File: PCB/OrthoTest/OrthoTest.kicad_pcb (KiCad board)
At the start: 2 copper layers, 3.6 x 3.3 mm, 182 parts, among them SW1 SW_Push, SW10 SW_Push, SW11 SW_Push, SW12 SW_Push, SW13 SW_Push, SW14 SW_Push, SW15 SW_Push, SW16 SW_Push, SW17 SW_Push, SW18 SW_Push, SW19 SW_Push, SW2 SW_Push, SW20 SW_Push, SW21 SW_Push, SW22 SW_Push, SW23 SW_Push, SW24 SW_Push, SW25 SW_Push, SW26 SW_Push, SW27 SW_Push, SW28 SW_Push, SW29 SW_Push, SW3 SW_Push, SW30 SW_Push, SW31 SW_Push, SW32 SW_Push, SW33 SW_Push, SW34 SW_Push, SW35 SW_Push, SW36 SW_Push, SW37 SW_Push, SW38 SW_Push, SW39 SW_Push, SW4 SW_Push, SW40 SW_Push, SW41 SW_Push, SW42 SW_Push, SW43 SW_Push, SW44 SW_Push, SW45 SW_Push, SW46 SW_Push, SW47 SW_Push, SW48 SW_Push, SW49 SW_Push, SW5 SW_Push, SW50 SW_Push, SW51 SW_Push, SW52 SW_Push, SW53 SW_Push, SW54 SW_Push, SW55 SW_Push, SW56 SW_Push, SW57 SW_Push, SW58 SW_Push, SW59 SW_Push, SW6 SW_Push, SW60 RotaryEncoder_Switch_MP, SW61 RotaryEncoder_Switch_MP, SW7 SW_Push, SW8 SW_Push, SW9 SW_Push

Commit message: added libraries and placed pcb components
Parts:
- A1: footprint Module:RaspberryPi_Pico_Common_SMD -> Module:RaspberryPi_Pico_Common_THT
- D1, D10, D11, D12, D13, D14, D15, D16, D17, D18, D19, D2, D20, D21, D22, D23, D24, D25, D26, D27, D28, D29, D3, D30, D31, D32, D33, D34, D35, D36, D37, D38, D39, D4, D40, D41, D42, D43, D44, D45, D46, D47, D48, D49, D5, D50, D51, D52, D53, D54, D55, D56, D57, D58, D59, D6, D7, D8, D9, LED1, LED10, LED11, LED12, LED13, LED14, LED15, LED16, LED17, LED18, LED19, LED2, LED20, LED21, LED22, LED23, LED24, LED25, LED26, LED27, LED28, LED29, LED3, LED30, LED31, LED32, LED33, LED34, LED35, LED36, LED37, LED38, LED39, LED4, LED40, LED41, LED42, LED43, LED44, LED45, LED46, LED47, LED48, LED49, LED5, LED50, LED51, LED52, LED53, LED54, LED55, LED56, LED57, LED58, LED59, LED6, LED7, LED8, LED9: moved to B.Cu
- moved LED12 447.3 mm to (251.4, 36.6)
- moved LED24 432.7 mm to (251.4, 55.7)
- moved LED11 427.7 mm to (232.3, 36.6)
- moved LED36 418.7 mm to (251.4, 74.8)
- moved LED23 413.0 mm to (232.3, 55.7)
- moved LED10 408.0 mm to (213.3, 36.6)
- moved LED48 405.3 mm to (251.4, 93.8)
- moved D12 400.7 mm to (255.8, 49.1), turned to 135 degrees
- moved LED35 399.0 mm to (232.3, 74.8)
- moved LED22 393.4 mm to (213.3, 55.7)
- moved LED59 391.6 mm to (251.4, 112.8)
- moved D24 389.9 mm to (255.8, 68.2), turned to 135 degrees
- moved LED9 388.4 mm to (194.2, 36.6)
- moved SW48 386.2 mm to (251.3, 98.5)
- moved SW12 386.1 mm to (251.3, 41.4)
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- renumbered S1 to S54
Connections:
- SW60 pad A: unconnected-(SW60-PadA) -> (no net)
- SW60 pad B: unconnected-(SW60-PadB) -> (no net)
- SW60 pad C: GND -> (no net)
- SW60 pad MP: unconnected-(SW60-PadMP) -> (no net)
- SW60 pad S1: unconnected-(SW60-PadS1) -> (no net)
- SW60 pad S2: unconnected-(SW60-PadS2) -> (no net)
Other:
- board size 3.6 x 3.3 mm -> 228.6 x 127.2 mm
- board text added: "Raspberry Pi Pico"

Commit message: finished routing pcb
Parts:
- added D60: D, MyKeebLib:D_SOD-123_SmallArrow, F.Cu at (266.0, 34.1)
- added D61: D, MyKeebLib:D_SOD-123_SmallArrow, F.Cu at (236.9, 34.1)
- moved D40 27.7 mm to (113.2, 132.2)
- moved D42 27.7 mm to (151.2, 132.2)
- moved D43 27.7 mm to (170.3, 132.2)
- moved D45 27.7 mm to (208.4, 132.2)
- moved D47 27.7 mm to (246.5, 132.2)
- moved D48 27.7 mm to (265.6, 132.2)
- moved LED26 27.7 mm to (70.7, 100.7)
- moved LED30 27.7 mm to (146.9, 100.7)
- moved LED32 27.7 mm to (185.0, 100.7)
- moved LED33 27.7 mm to (204.1, 100.7)
- moved LED35 27.7 mm to (242.2, 100.7)
- moved LED38 27.7 mm to (70.7, 119.7)
- moved LED42 27.7 mm to (146.9, 119.7)
- moved LED44 27.7 mm to (185.0, 119.7)
- moved LED45 27.7 mm to (204.1, 119.7)
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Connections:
- A1 pad 1: unconnected-(A1-GPIO0-Pad1) -> col0
- A1 pad 10: unconnected-(A1-GPIO7-Pad10) -> col7
- A1 pad 11: unconnected-(A1-GPIO8-Pad11) -> col8
- A1 pad 12: unconnected-(A1-GPIO9-Pad12) -> col9
- A1 pad 13: Net-(A1-GND-Pad13) -> GND
- A1 pad 14: unconnected-(A1-GPIO10-Pad14) -> col10
- A1 pad 15: unconnected-(A1-GPIO11-Pad15) -> col11
- A1 pad 16: unconnected-(A1-GPIO12-Pad16) -> ec1_b
- A1 pad 17: unconnected-(A1-GPIO13-Pad17) -> ec1_a
- A1 pad 18: Net-(A1-GND-Pad13) -> GND
- A1 pad 19: unconnected-(A1-GPIO14-Pad19) -> ec2_a
- A1 pad 2: unconnected-(A1-GPIO1-Pad2) -> col1
- A1 pad 20: unconnected-(A1-GPIO15-Pad20) -> ec2_b
- A1 pad 21: unconnected-(A1-GPIO16-Pad21) -> oled_cl
- A1 pad 22: unconnected-(A1-GPIO17-Pad22) -> oled_data
- A1 pad 23: Net-(A1-GND-Pad13) -> GND
- A1 pad 24: unconnected-(A1-GPIO18-Pad24) -> ec_col0
- A1 pad 25: unconnected-(A1-GPIO19-Pad25) -> ec_col1
- A1 pad 26: unconnected-(A1-GPIO20-Pad26) -> ec_row0
- A1 pad 27: unconnected-(A1-GPIO21-Pad27) -> row4
- A1 pad 28: Net-(A1-GND-Pad13) -> GND
- A1 pad 29: unconnected-(A1-GPIO22-Pad29) -> row3
- A1 pad 3: Net-(A1-GND-Pad13) -> GND
- A1 pad 31: unconnected-(A1-GPIO26_ADC0-Pad31) -> row2
- A1 pad 32: unconnected-(A1-GPIO27_ADC1-Pad32) -> row1
- A1 pad 33: unconnected-(A1-AGND-Pad33) -> GND
- A1 pad 34: unconnected-(A1-GPIO28_ADC2-Pad34) -> row0
- A1 pad 35: unconnected-(A1-ADC_VREF-Pad35) -> led_data
- A1 pad 36: unconnected-(A1-3V3-Pad36) -> +3V3
- A1 pad 38: Net-(A1-GND-Pad13) -> GND
- A1 pad 4: unconnected-(A1-GPIO2-Pad4) -> col2
- A1 pad 40: unconnected-(A1-VBUS-Pad40) -> +5V
- A1 pad 5: unconnected-(A1-GPIO3-Pad5) -> col3
- A1 pad 6: unconnected-(A1-GPIO4-Pad6) -> col4
- A1 pad 7: unconnected-(A1-GPIO5-Pad7) -> col5
- A1 pad 8: Net-(A1-GND-Pad13) -> GND
- A1 pad 9: unconnected-(A1-GPIO6-Pad9) -> col6
- SW60 pad A: (no net) -> ec1_a
- SW60 pad B: (no net) -> ec1_b
- SW60 pad C: (no net) -> GND
- SW60 pad MP: (no net) -> GND
- SW60 pad S1: (no net) -> ec_col0
- SW60 pad S2: (no net) -> Net-(D60-A)
- SW61 pad A: unconnected-(SW61-PadA) -> ec2_a
- SW61 pad B: unconnected-(SW61-PadB) -> ec2_b
- SW61 pad MP: unconnected-(SW61-PadMP) -> GND
- SW61 pad S1: unconnected-(SW61-PadS1) -> ec_col1
- SW61 pad S2: unconnected-(SW61-PadS2) -> Net-(D61-A)
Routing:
- net +5V: track 0.00 -> 1596.4 mm, vias 0 -> 61
- net row4: track 0.00 -> 350.5 mm, vias 0 -> 8
- net row3: track 0.00 -> 329.8 mm, vias 0 -> 6
- net row2: track 0.00 -> 315.1 mm, vias 0 -> 4
- net row1: track 0.00 -> 298.0 mm, vias 0 -> 2
- net row0: track 0.00 -> 283.2 mm
- net col11: track 0.00 -> 276.4 mm
- net col10: track 0.00 -> 260.2 mm
- net col9: track 0.00 -> 246.3 mm
- net Net-(LED48-DOUT): track 0.00 -> 246.2 mm, vias 0 -> 2
- net Net-(LED36-DOUT): track 0.00 -> 245.3 mm, vias 0 -> 2
- net Net-(LED24-DOUT): track 0.00 -> 244.9 mm, vias 0 -> 2
- net Net-(LED12-DOUT): track 0.00 -> 244.0 mm, vias 0 -> 2
- net col8: track 0.00 -> 230.1 mm
- net col7: track 0.00 -> 214.0 mm
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- added copper zone on B.Cu, net GND
- added copper zone on F.Cu, net GND

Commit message: fixed ucontroller usb c position and added grounding vias
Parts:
- added C1: 100n, Capacitor_SMD:C_0603_1608Metric, B.Cu at (56.1, 65.9)
- added C10: 100n, Capacitor_SMD:C_0603_1608Metric, B.Cu at (227.6, 65.9)
- added C11: 100n, Capacitor_SMD:C_0603_1608Metric, B.Cu at (246.6, 65.9)
- added C12: 100n, Capacitor_SMD:C_0603_1608Metric, B.Cu at (265.0, 67.2)
- added C13: 100n, Capacitor_SMD:C_0603_1608Metric, B.Cu at (56.1, 85.0)
- added C14: 100n, Capacitor_SMD:C_0603_1608Metric, B.Cu at (75.2, 85.0)
- added C15: 100n, Capacitor_SMD:C_0603_1608Metric, B.Cu at (94.2, 85.0)
- added C16: 100n, Capacitor_SMD:C_0603_1608Metric, B.Cu at (113.2, 85.0)
- added C17: 100n, Capacitor_SMD:C_0603_1608Metric, B.Cu at (132.3, 85.0)
- added C18: 100n, Capacitor_SMD:C_0603_1608Metric, B.Cu at (151.3, 85.0)
- added C19: 100n, Capacitor_SMD:C_0603_1608Metric, B.Cu at (170.4, 85.0)
- added C2: 100n, Capacitor_SMD:C_0603_1608Metric, B.Cu at (75.2, 65.9)
- added C20: 100n, Capacitor_SMD:C_0603_1608Metric, B.Cu at (189.4, 85.0)
- added C21: 100n, Capacitor_SMD:C_0603_1608Metric, B.Cu at (208.5, 85.0)
- added C22: 100n, Capacitor_SMD:C_0603_1608Metric, B.Cu at (227.6, 85.0)
- added C23: 100n, Capacitor_SMD:C_0603_1608Metric, B.Cu at (246.6, 85.0)
- added C24: 100n, Capacitor_SMD:C_0603_1608Metric, B.Cu at (265.0, 86.3)
- added C25: 100n, Capacitor_SMD:C_0603_1608Metric, B.Cu at (56.1, 104.0)
- added C26: 100n, Capacitor_SMD:C_0603_1608Metric, B.Cu at (75.2, 104.0)
- added C27: 100n, Capacitor_SMD:C_0603_1608Metric, B.Cu at (94.2, 104.0)
- added C28: 100n, Capacitor_SMD:C_0603_1608Metric, B.Cu at (113.2, 104.0)
- added C29: 100n, Capacitor_SMD:C_0603_1608Metric, B.Cu at (132.3, 104.0)
- added C3: 100n, Capacitor_SMD:C_0603_1608Metric, B.Cu at (94.2, 65.9)
- added C30: 100n, Capacitor_SMD:C_0603_1608Metric, B.Cu at (151.3, 104.0)
- added C31: 100n, Capacitor_SMD:C_0603_1608Metric, B.Cu at (170.4, 104.0)
- added C32: 100n, Capacitor_SMD:C_0603_1608Metric, B.Cu at (189.4, 104.0)
- added C33: 100n, Capacitor_SMD:C_0603_1608Metric, B.Cu at (208.5, 104.0)
- added C34: 100n, Capacitor_SMD:C_0603_1608Metric, B.Cu at (227.6, 104.0)
- added C35: 100n, Capacitor_SMD:C_0603_1608Metric, B.Cu at (246.6, 104.0)
- added C36: 100n, Capacitor_SMD:C_0603_1608Metric, B.Cu at (265.0, 105.3)
- added C37: 100n, Capacitor_SMD:C_0603_1608Metric, B.Cu at (56.1, 123.0)
- added C38: 100n, Capacitor_SMD:C_0603_1608Metric, B.Cu at (75.2, 123.0)
- added C39: 100n, Capacitor_SMD:C_0603_1608Metric, B.Cu at (94.2, 123.0)
- added C4: 100n, Capacitor_SMD:C_0603_1608Metric, B.Cu at (113.2, 65.9)
- added C40: 100n, Capacitor_SMD:C_0603_1608Metric, B.Cu at (113.2, 123.0)
- added C41: 100n, Capacitor_SMD:C_0603_1608Metric, B.Cu at (132.3, 123.0)
- added C42: 100n, Capacitor_SMD:C_0603_1608Metric, B.Cu at (151.3, 123.0)
- added C43: 100n, Capacitor_SMD:C_0603_1608Metric, B.Cu at (170.4, 123.0)
- added C44: 100n, Capacitor_SMD:C_0603_1608Metric, B.Cu at (189.4, 123.0)
- added C45: 100n, Capacitor_SMD:C_0603_1608Metric, B.Cu at (208.5, 123.0)
- added C46: 100n, Capacitor_SMD:C_0603_1608Metric, B.Cu at (227.6, 123.0)
- added C47: 100n, Capacitor_SMD:C_0603_1608Metric, B.Cu at (246.6, 123.0)
- added C48: 100n, Capacitor_SMD:C_0603_1608Metric, B.Cu at (265.0, 124.4)
- added C49: 100n, Capacitor_SMD:C_0603_1608Metric, B.Cu at (56.1, 142.1)
- added C5: 100n, Capacitor_SMD:C_0603_1608Metric, B.Cu at (132.3, 65.9)
- added C50: 100n, Capacitor_SMD:C_0603_1608Metric, B.Cu at (75.2, 142.1)
- added C51: 100n, Capacitor_SMD:C_0603_1608Metric, B.Cu at (94.2, 142.1)
- added C52: 100n, Capacitor_SMD:C_0603_1608Metric, B.Cu at (113.2, 142.1)
- added C53: 100n, Capacitor_SMD:C_0603_1608Metric, B.Cu at (132.3, 142.1)
- added C54: 100n, Capacitor_SMD:C_0603_1608Metric, B.Cu at (160.9, 142.1)
- added C55: 100n, Capacitor_SMD:C_0603_1608Metric, B.Cu at (189.4, 142.1)
- added C56: 100n, Capacitor_SMD:C_0603_1608Metric, B.Cu at (208.5, 142.1)
- added C57: 100n, Capacitor_SMD:C_0603_1608Metric, B.Cu at (227.6, 142.1)
- added C58: 100n, Capacitor_SMD:C_0603_1608Metric, B.Cu at (246.6, 142.1)
- added C59: 100n, Capacitor_SMD:C_0603_1608Metric, B.Cu at (265.6, 142.1)
- added C6: 100n, Capacitor_SMD:C_0603_1608Metric, B.Cu at (151.3, 65.9)
- added C7: 100n, Capacitor_SMD:C_0603_1608Metric, B.Cu at (170.4, 65.9)
- added C8: 100n, Capacitor_SMD:C_0603_1608Metric, B.Cu at (189.4, 65.9)
- added C9: 100n, Capacitor_SMD:C_0603_1608Metric, B.Cu at (208.5, 65.9)
- added H1: MountingHolePlate, MyKeebLib:Spacer_3.2mm, F.Cu at (80.2, 86.3)
- added H2: MountingHolePlate, MyKeebLib:Spacer_3.2mm, F.Cu at (80.2, 124.4)
- added H3: MountingHolePlate, MyKeebLib:Spacer_3.2mm, F.Cu at (156.4, 86.3)
- added H4: MountingHolePlate, MyKeebLib:Spacer_3.2mm, F.Cu at (156.4, 128.4)
- added H5: MountingHolePlate, MyKeebLib:Spacer_3.2mm, F.Cu at (232.6, 86.3)
- added H6: MountingHolePlate, MyKeebLib:Spacer_3.2mm, F.Cu at (232.6, 124.4)
- moved A1 5.00 mm to (38.7, 53.3)
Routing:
- net +5V: track 1596.4 -> 1756.8 mm
- net oled_data: track 89.1 -> 94.1 mm
- net oled_cl: track 85.5 -> 90.5 mm
- net ec1_b: track 175.7 -> 180.7 mm
- net ec1_a: track 174.9 -> 179.9 mm
- net ec2_b: track 135.8 -> 140.8 mm
- net +3V3: track 138.0 -> 143.0 mm
- net ec2_a: track 141.7 -> 146.4 mm
- net ec_col1: track 163.8 -> 168.2 mm
- net ec_col0: track 198.1 -> 202.5 mm
- net ec_row0: track 190.1 -> 194.4 mm
- net col11: track 276.4 -> 280.6 mm
- net col10: track 260.2 -> 264.1 mm
- net col9: track 246.3 -> 250.0 mm
- net row3: track 329.8 -> 333.5 mm
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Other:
- board size 228.6 x 127.2 mm -> 233.7 x 127.2 mm

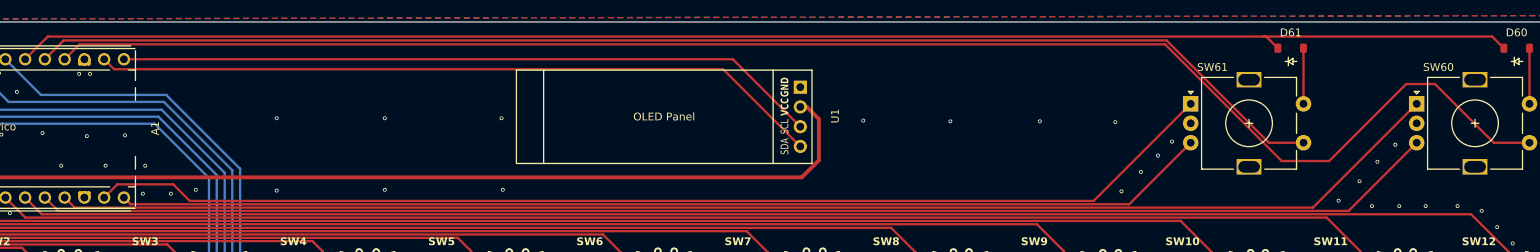
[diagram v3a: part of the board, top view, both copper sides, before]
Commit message: spaced encoders additional 10mm aparart
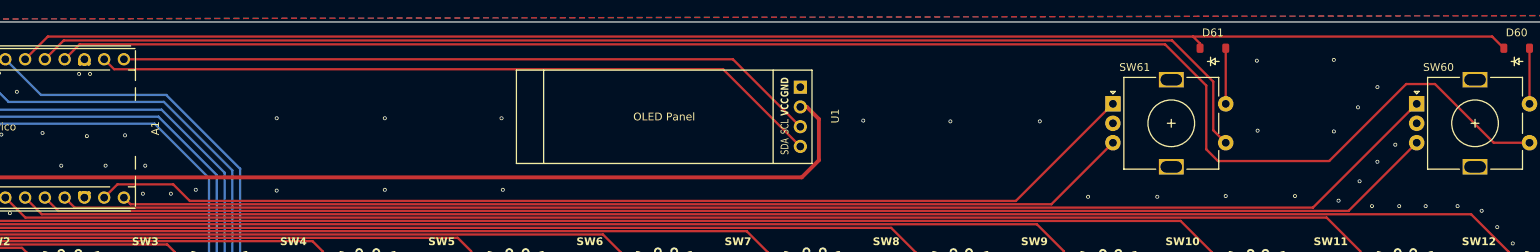
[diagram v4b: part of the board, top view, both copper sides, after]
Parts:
- moved D61 10.0 mm to (226.9, 34.1)
- moved SW61 10.0 mm to (214.1, 41.2)
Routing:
- net ec2_a: track 146.4 -> 136.4 mm
- net ec2_b: track 140.8 -> 130.8 mm
- net ec_col1: track 168.2 -> 161.9 mm
- net ec_col0: track 202.5 -> 207.3 mm
- net ec_row0: track 194.4 -> 193.8 mm
- net GND: vias 313 -> 318
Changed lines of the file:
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@@
 	(footprint "MyKeebLib:D_SOD-123_SmallArrow"
 		(layer "F.Cu")
-		(at 236.95 34.1)
+		(at 226.95 34.1)
 		(descr "SOD-123")
 		(tags "SOD-123")
@@
 	(footprint "Rotary_Encoder:RotaryEncoder_Alps_EC11E-Switch_Vertical_H20mm"
 		(layer "F.Cu")
-		(at 224.1 41.25)
+		(at 214.1 41.25)
 		(descr "Alps rotary encoder, EC12E... with switch, vertical shaft, http://www.alps.com/prod/info/E/HTML/Encoder/Incremental/EC11/EC11E15204A3.html")
 		(tags "rotary encoder")
@@
 	)
 	(segment
-		(start 267.65 46.25)
-		(end 263.05 46.25)
+		(start 226.1 38.9)
+		(end 220.8 33.6)
+		(width 0.3)
+		(layer "F.Cu")
+		(net 3)
+	)
+	(segment
+		(start 263.05 46.25)
+		(end 255.5 38.7)
+		(width 0.3)
+		(layer "F.Cu")
+		(net 3)
+	)
+	(segment
+		(start 255.5 38.7)
+		(end 251.8 38.7)
 		(width 0.3)
 		(layer "F.Cu")
@@
 	)
 	(segment
-		(start 220.8 33.6)
-		(end 81.26 33.6)
+		(start 226.1 47.1)
+		(end 226.1 38.9)
 		(width 0.3)
 		(layer "F.Cu")
@@
 	)
 	(segment
-		(start 263.05 46.25)
-		(end 255.5 38.7)
+		(start 267.65 46.25)
+		(end 263.05 46.25)
 		(width 0.3)
 		(layer "F.Cu")
@@
 	)
 	(segment
-		(start 235.8 48.6)
-		(end 220.8 33.6)
+		(start 227.6 48.6)
+		(end 226.1 47.1)
 		(width 0.3)
 		(layer "F.Cu")
@@
 	(segment
 		(start 241.9 48.6)
-		(end 235.8 48.6)
+		(end 227.6 48.6)
 		(width 0.3)
 		(layer "F.Cu")
@@
 	)
 	(segment
-		(start 255.5 38.7)
-		(end 251.8 38.7)
+		(start 220.8 33.6)
+		(end 81.26 33.6)
 		(width 0.3)
 		(layer "F.Cu")
@@
 	)
 	(segment
-		(start 224.1 46.25)
-		(end 216.19 54.16)
+		(start 206.19 54.16)
+		(end 87.82 54.16)
 		(width 0.3)
 		(layer "F.Cu")
@@
 	)
 	(segment
-		(start 87.82 54.16)
-		(end 86.96 53.3)
+		(start 214.1 46.25)
+		(end 206.19 54.16)
 		(width 0.3)
 		(layer "F.Cu")
@@
 	)
 	(segment
-		(start 216.19 54.16)
-		(end 87.82 54.16)
+		(start 87.82 54.16)
+		(end 86.96 53.3)
 		(width 0.3)
 		(layer "F.Cu")
@@
 	)
 	(segment
-		(start 234.15 46.25)
-		(end 221 33.1)
+		(start 227 38.4)
+		(end 221.7 33.1)
 		(width 0.3)
 		(layer "F.Cu")
@@
 	)
 	(segment
-		(start 221 33.1)
+		(start 221.7 33.1)
 		(end 79.22 33.1)
 		(width 0.3)
@@
 	)
 	(segment
-		(start 238.6 46.25)
-		(end 234.15 46.25)
+		(start 227 44.65)
+		(end 227 38.4)
+		(width 0.3)
+		(layer "F.Cu")
+		(net 6)
+	)
+	(segment
+		(start 228.6 46.25)
+		(end 227 44.65)
 		(width 0.3)
 		(layer "F.Cu")
@@
 	)
 	(segment
-		(start 211.618 53.732)
-		(end 95.432 53.732)
+		(start 214.1 41.25)
+		(end 201.618 53.732)
 		(width 0.3)
 		(layer "F.Cu")
@@
 	)
 	(segment
-		(start 224.1 41.25)
-		(end 211.618 53.732)
+		(start 201.618 53.732)
+		(end 95.432 53.732)
 		(width 0.3)
 		(layer "F.Cu")
@@
 	)
 	(segment
-		(start 233.4 32.6)
-		(end 77.18 32.6)
+		(start 225.3 34.1)
+		(end 225.3 33.5)
 		(width 0.3)
 		(layer "F.Cu")
@@
 	)
 	(segment
-		(start 233.8 32.6)
-		(end 233.4 32.6)
+		(start 262.85 32.6)
+		(end 224.4 32.6)
 		(width 0.3)
 		(layer "F.Cu")
@@
 	)
 	(segment
-		(start 264.35 34.1)
-		(end 262.85 32.6)
+		(start 224.4 32.6)
+		(end 77.18 32.6)
 		(width 0.3)
 		(layer "F.Cu")
@@
 	)
 	(segment
-		(start 262.85 32.6)
-		(end 233.4 32.6)
+		(start 225.3 33.5)
+		(end 224.4 32.6)
 		(width 0.3)
 		(layer "F.Cu")
@@
 	)
 	(segment
-		(start 77.18 32.6)
-		(end 74.26 35.52)
+		(start 264.35 34.1)
+		(end 262.85 32.6)
 		(width 0.3)
 		(layer "F.Cu")
@@
 	)
 	(segment
-		(start 235.3 34.1)
-		(end 233.8 32.6)
+		(start 77.18 32.6)
+		(end 74.26 35.52)
 		(width 0.3)
 		(layer "F.Cu")
@@
 	)
 	(segment
-		(start 238.6 41.25)
-		(end 238.6 34.1)
+		(start 228.6 40.794716)
+		(end 228.827642 41.022358)
+		(width 0.3)
+		(layer "F.Cu")
+		(net 10)
+	)
+	(segment
+		(start 228.6 34.1)
+		(end 228.6 40.794716)
 		(width 0.3)
 		(layer "F.Cu")
@@
 	)
 	(via
+		(at 245.6 41.7)
+		(size 0.5)
+		(drill 0.3)
+		(layers "F.Cu" "B.Cu")
+		(free yes)
+		(net 79)
+	)
+	(via
 		(at 62.4 63.1)
 		(size 1)
@@
 	)
 	(via
+		(at 248.1 39.1)
+		(size 0.5)
+		(drill 0.3)
+		(layers "F.Cu" "B.Cu")
+		(free yes)
+		(net 79)
+	)
+	(via
 		(at 54.8 48.8)
 		(size 0.5)
@@
 	)
 	(via
-		(at 217.7 50)
-		(size 0.5)
-		(drill 0.3)
-		(layers "F.Cu" "B.Cu")
-		(free yes)
-		(net 79)
-	)
-	(via
 		(at 209.3 64.8)
 		(size 0.5)
@@
 	)
 	(via
+		(at 242.5 35.6)
+		(size 0.5)
+		(drill 0.3)
+		(layers "F.Cu" "B.Cu")
+		(free yes)
+		(net 79)
+	)
+	(via
 		(at 94.5 144.6)
 		(size 0.5)
@@
 	)
 	(via
+		(at 210.9 53.2)
+		(size 0.5)
+		(drill 0.3)
+		(layers "F.Cu" "B.Cu")
+		(free yes)
+		(net 79)
+	)
+	(via
 		(at 266.5 141)
 		(size 0.5)
@@
 	)
 	(via
+		(at 232.6 35.7)
+		(size 0.5)
+		(drill 0.3)
+		(layers "F.Cu" "B.Cu")
+		(free yes)
+		(net 79)
+	)
+	(via
 		(at 68.9 40.1)
 		(size 0.5)
@@
 	)
 	(via
+		(at 219.8 53.2)
+		(size 0.5)
+		(drill 0.3)
+		(layers "F.Cu" "B.Cu")
+		(free yes)
+		(net 79)
+	)
+	(via
 		(at 266.1 87.2)
 		(size 0.5)
@@
 	)
 	(via
+		(at 228.6 53.1)
+		(size 0.5)
+		(drill 0.3)
+		(layers "F.Cu" "B.Cu")
+		(free yes)
+		(net 79)
+	)
+	(via
 		(at 252.8 98.4)
 		(size 1)
@@
 	)
 	(via
-		(at 219.9 47.9)
-		(size 0.5)
-		(drill 0.3)
-		(layers "F.Cu" "B.Cu")
-		(free yes)
-		(net 79)
-	)
-	(via
 		(at 56.3 87.6)
 		(size 0.5)
@@
 	)
 	(via
+		(at 242.5 44.8)
+		(size 0.5)
+		(drill 0.3)
+		(layers "F.Cu" "B.Cu")
+		(free yes)
+		(net 79)
+	)
+	(via
 		(at 43.1 44.5)
 		(size 0.5)
@@
 	)
 	(via
-		(at 261.5 55)
+		(at 232.7 44.7)
 		(size 0.5)
 		(drill 0.3)
@@
 	)
 	(via
-		(at 81.4 136.9)
-		(size 1)
-		(drill 0.5)
+		(at 261.5 55)
+		(size 0.5)
+		(drill 0.3)
 		(layers "F.Cu" "B.Cu")
 		(free yes)
@@
 	)
 	(via
-		(at 171.2 102.8)
-		(size 0.5)
-		(drill 0.3)
+		(at 81.4 136.9)
+		(size 1)
+		(drill 0.5)
 		(layers "F.Cu" "B.Cu")
 		(free yes)
@@
 	)
 	(via
-		(at 215.2 52.5)
+		(at 171.2 102.8)
 		(size 0.5)
 		(drill 0.3)
@@
 	)
 	(via
-		(at 214.4 43.6)
-		(size 0.5)
-		(drill 0.3)
-		(layers "F.Cu" "B.Cu")
-		(free yes)
-		(net 79)
-	)
-	(via
 		(at 119.3 105.5)
 		(size 1)
@@
 	)
 	(via
-		(at 221.7 46.1)
+		(at 135.669059 52.3)
 		(size 0.5)
 		(drill 0.3)
@@
 	)
 	(via
-		(at 135.669059 52.3)
-		(size 0.5)
-		(drill 0.3)
+		(at 176.5 145.3)
+		(size 1)
+		(drill 0.5)
 		(layers "F.Cu" "B.Cu")
 		(free yes)
@@
 	)
 	(via
-		(at 176.5 145.3)
-		(size 1)
-		(drill 0.5)
+		(at 237.5 53.1)
+		(size 0.5)
+		(drill 0.3)
 		(layers "F.Cu" "B.Cu")
 		(free yes)
